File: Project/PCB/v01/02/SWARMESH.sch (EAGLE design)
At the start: 48 parts, among them IC1 4051N, M1 MOTOR10MM, M2 MOTOR10MM, Q1 TIP122, U1 ESP32DEVKITC, U2 TCRT5000L, U3 L293D, U4 7805T, U5 TCRT5000L

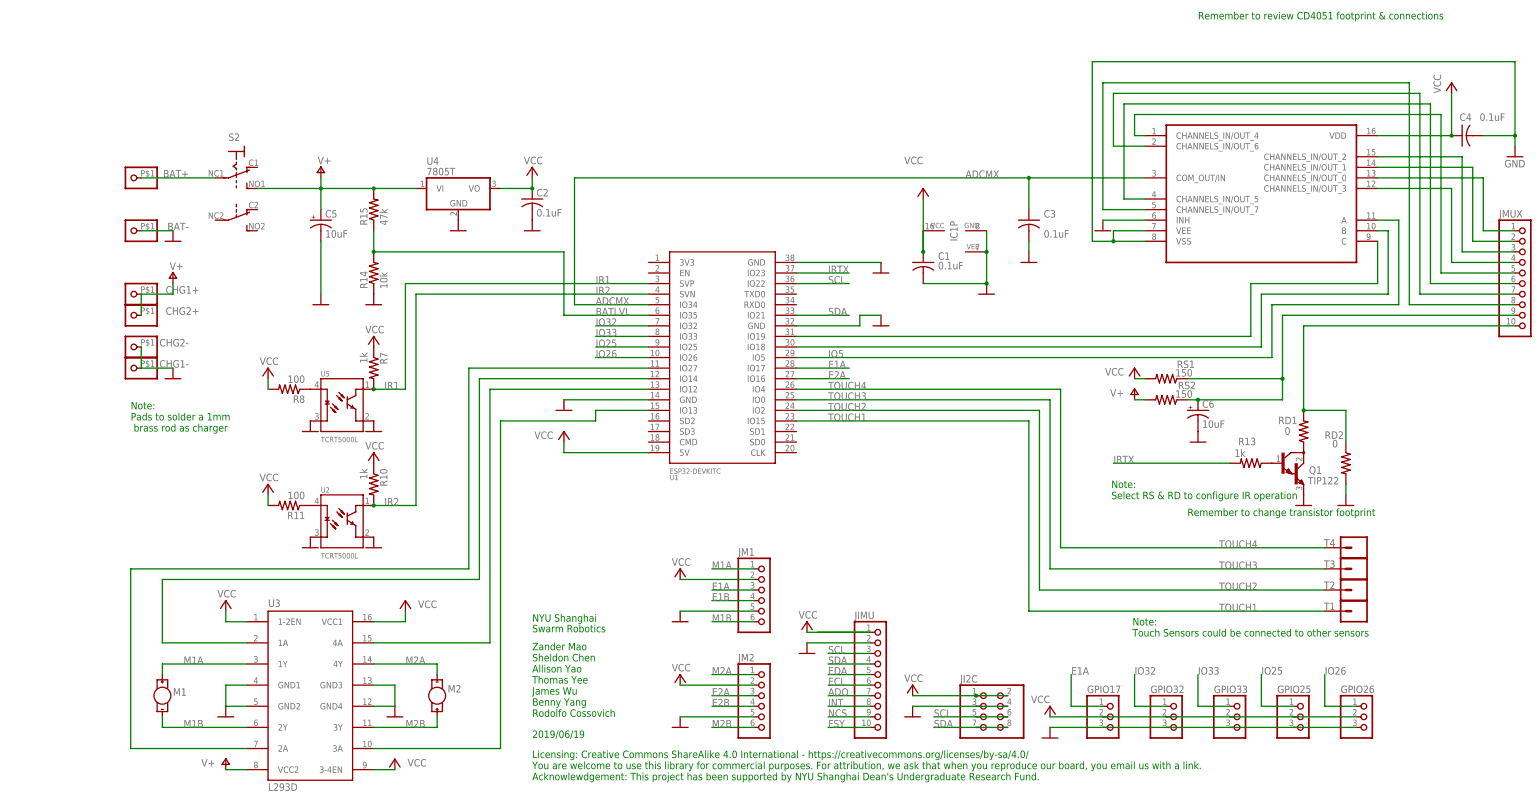
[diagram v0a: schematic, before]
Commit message: update schematic
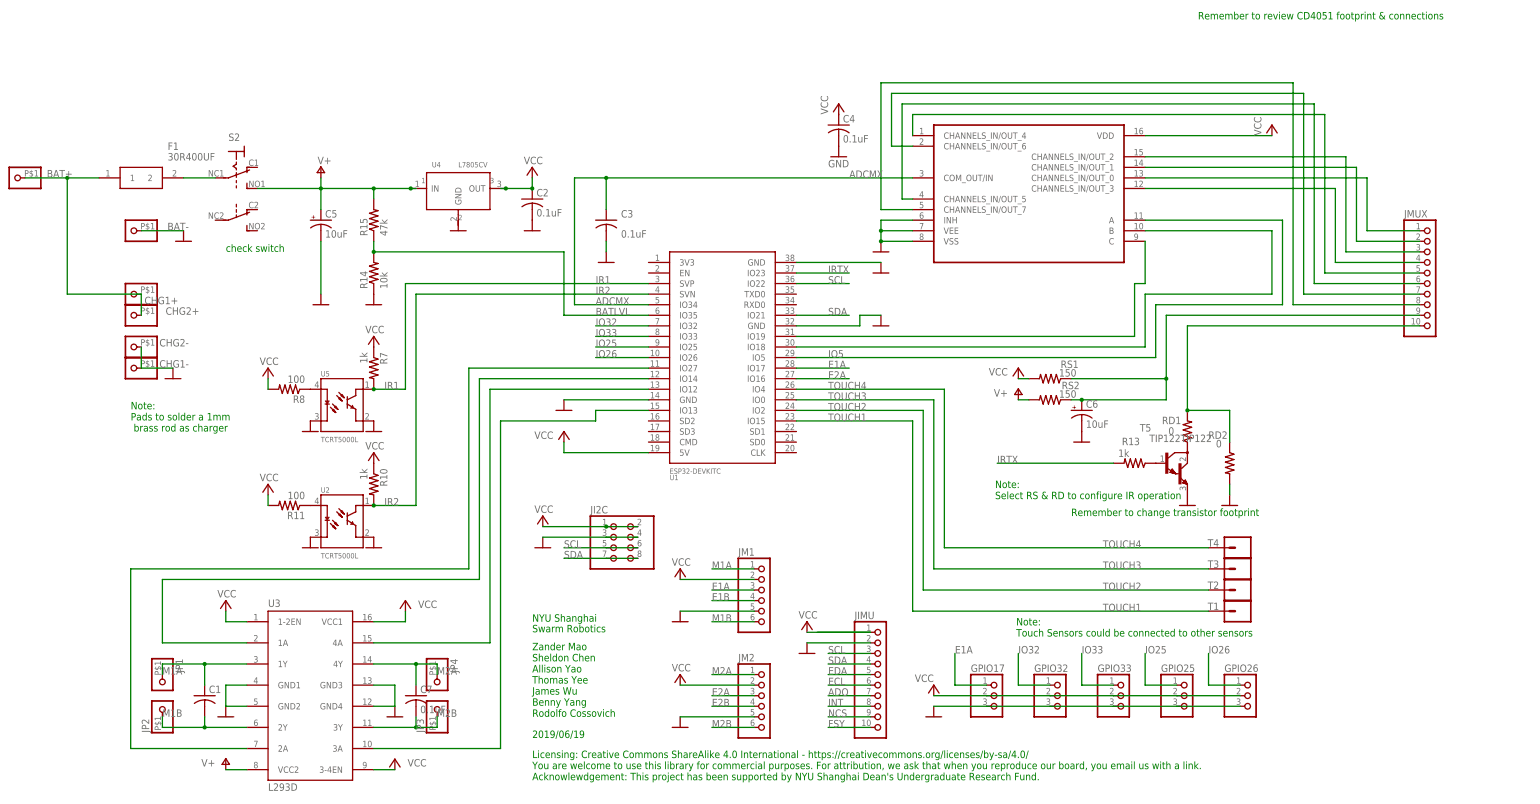
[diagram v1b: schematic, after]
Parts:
- removed IC1: 4051N, 40xx:4051N
- removed M1, M2: MOTOR10MM, SparkFun-Electromechanical:MOTOR10MM
- removed Q1: TIP122, transistor-npn:TIP122
- added C7: 0.1uF, adafruit:C-US050-024X044
- added F1: 30R400UF, 30R400UF:30R400UF
- added JP1, JP2, JP3, JP4: (no value), adafruit:PINHD-1X1-BIGPOGO
- added T5: TIP122TIP122, TIP122(2):TIP122TIP122
- C4: device adafruit:C-US050-024X044 -> rcl:C-US025-024X044
- R10, R11, R13, R14, R15, R7, R8, RD1, RD2, RS1, RS2: device adafruit:R-US_0207/12 -> adafruit:R-US_M0805
- U4: value 7805T -> L7805CV; device adafruit:7805T -> L7805:L7805CV
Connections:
- removed net N$21: BAT+.1, S21.P
- removed net N$37: Q1.C, RD1.1
- removed net N$38: R15.2
- new net N$12: R13.1, T5.B
- new net N$15: BAT+.1, CHG1+.1, CHG2+.1, F1.1
- new net N$18: F1.2, S21.P
- net GND: now also T5.E; no longer C1.2, IC1P.GND, IC1P.VEE, Q1.E, U4.GND
- net M1A: now also C1.1, JP1.1; no longer M1.+
- net M1B: now also C1.2, JP2.1; no longer M1.-
- net M2A: now also C7.1, JP4.1; no longer M2.-
- net M2B: now also C7.2, JP3.1; no longer M2.+
- net N$1: now also RD1.1, T5.C; no longer Q1.B, R13.1
- net V+: now also R15.2, U4.IN; no longer CHG1+.1, CHG2+.1, U4.VI
- net VCC: now also U4.OUT; no longer C1.1, IC1P.VCC, U4.VO
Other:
- note added: "check switch"
- moved on the sheet: BAT+, C1, C3, C4, C6, GPIO17, GPIO25, GPIO26, GPIO32, GPIO33, JI2C, JMUX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

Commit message: minor update
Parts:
- removed U$1: CD4051BEE4, CD4051BEE4:CD4051BEE4
- added U6: CD4051BEE4, CD4051BEE4:CD4051BEE4
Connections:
- removed net N$2: JMUX.1, U$1.CHANNELS_IN/OUT_0
- removed net N$3: JMUX.2, U$1.CHANNELS_IN/OUT_1
- removed net N$4: JMUX.3, U$1.CHANNELS_IN/OUT_2
- removed net N$6: JMUX.4, U$1.CHANNELS_IN/OUT_3
- new net ADCMX1: U6.COM_OUT/IN
- new net N$19: JMUX.1, U6.CHANNELS_IN/OUT_0
- new net N$20: JMUX.2, U6.CHANNELS_IN/OUT_1
- new net N$21: JMUX.4, U6.CHANNELS_IN/OUT_3
- new net N$22: JMUX.3, U6.CHANNELS_IN/OUT_2
- net ADCMX: no longer U$1.COM_OUT/IN
- net GND: no longer U$1.INH, U$1.VEE, U$1.VSS
- net IO5: now also U6.A; no longer U$1.A
- net N$11: now also U6.CHANNELS_IN/OUT_4; no longer U$1.CHANNELS_IN/OUT_4
- net N$12: now also U6.INH, U6.VEE, U6.VSS
- net N$13: now also U6.CHANNELS_IN/OUT_6; no longer U$1.CHANNELS_IN/OUT_6
- net N$14: now also U6.CHANNELS_IN/OUT_7; no longer U$1.CHANNELS_IN/OUT_7
- net N$5: now also U6.CHANNELS_IN/OUT_5; no longer U$1.CHANNELS_IN/OUT_5
- net N$7: now also U6.B; no longer U$1.B
- net N$8: now also U6.C; no longer U$1.C
- net VCC: now also U6.VDD; no longer U$1.VDD
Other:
- moved on the sheet: C6, JMUX, R13, RD1, RD2, RS1, RS2, T5

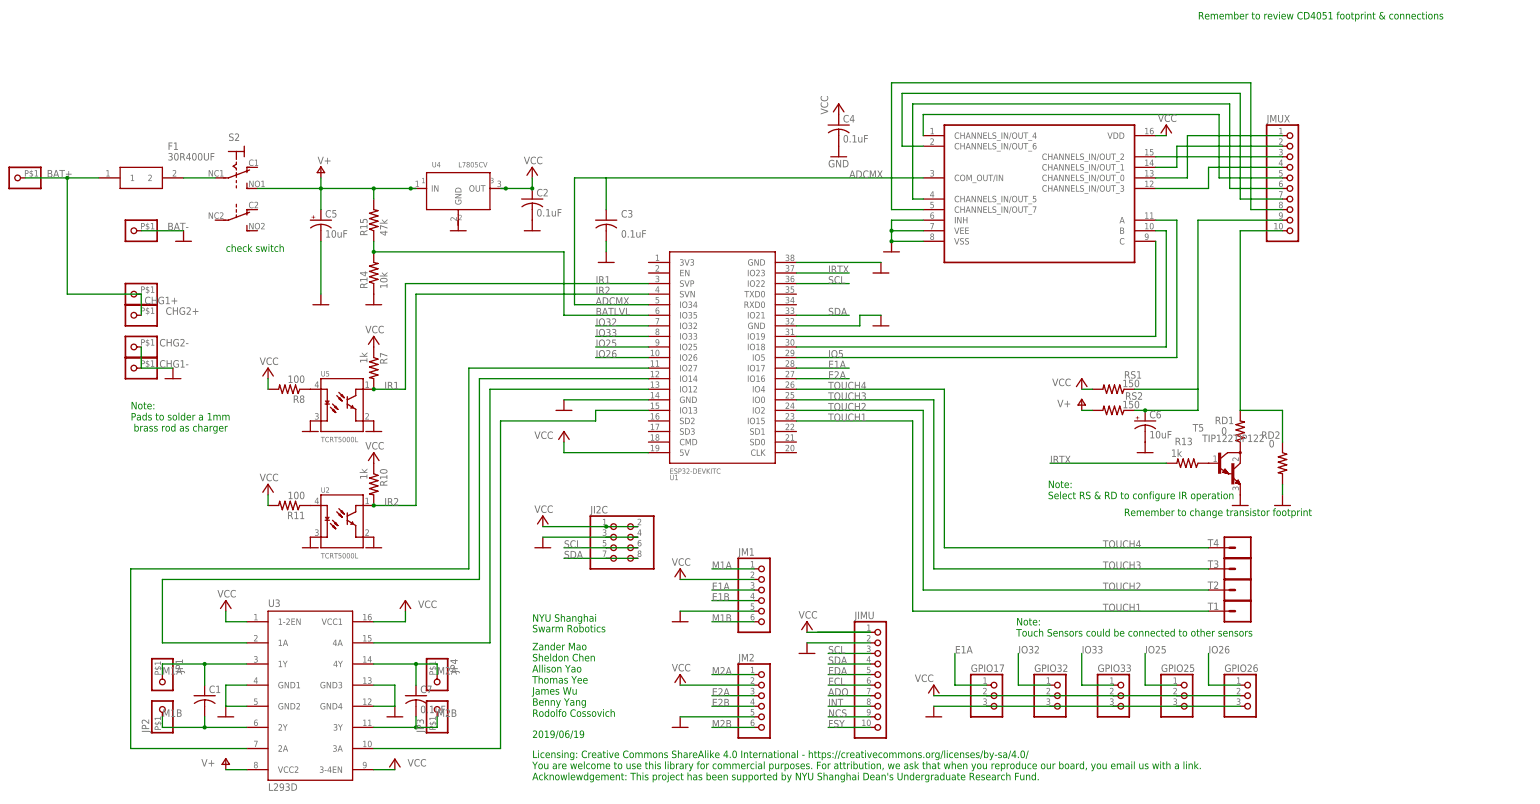
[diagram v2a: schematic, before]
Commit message: component placement
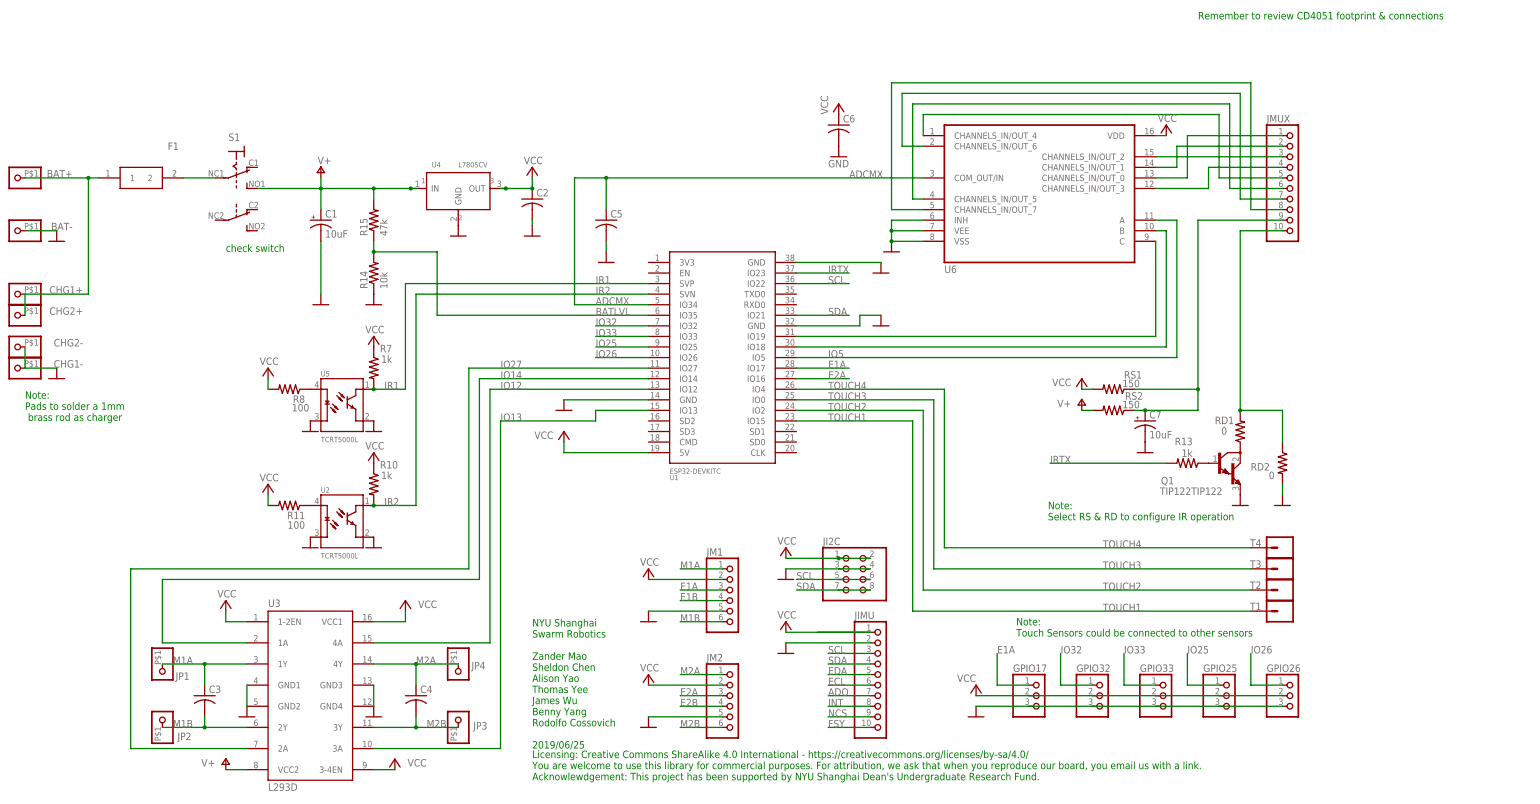
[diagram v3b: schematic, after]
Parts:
- C1, C7: value 0.1uF -> 10uF; device adafruit:C-US050-024X044 -> adafruit:CPOL-USE2.5-7
- C2, C3: value 0.1uF -> (none); device adafruit:C-US050-024X044 -> adafruit:C-USC0805
- C4: value 0.1uF -> (none); device rcl:C-US025-024X044 -> adafruit:C-USC0805
- C5, C6: value 10uF -> (none); device adafruit:CPOL-USE2.5-7 -> adafruit:C-USC0805
- renumbered S2 to S1, T5 to Q1
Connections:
- removed net ADCMX1: U6.COM_OUT/IN
- new net IO12: U1.IO12, U3.4A
- new net IO13: U1.IO13, U3.3A
- new net IO14: U1.IO14, U3.1A
- new net IO27: U1.IO27, U3.2A
- net ADCMX: now also C5.1, U6.COM_OUT/IN; no longer C3.1
- net GND: now also C1.-, C5.2, C6.2, C7.-, U4.GND; no longer C3.2, C4.2, C5.-, C6.-
- net IO5: no longer U1.IO12, U1.IO13, U1.IO14, U1.IO27, U3.1A, U3.2A, U3.3A, U3.4A
- net M1A: now also C3.1; no longer C1.1
- net M1B: now also C3.2; no longer C1.2
- net M2A: now also C4.1; no longer C7.1
- net M2B: now also C4.2; no longer C7.2
- net N$16: now also C7.+; no longer C6.+
- net V+: now also C1.+; no longer C5.+
- net VCC: now also C6.1; no longer C4.1
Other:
- note added: "NYU Shanghai Swarm Robotics Zander Mao Sheldon Chen Alison Yao Thomas Yee James Wu Benny Yang Rodolfo Cossovich 2019/06/25"
- note removed: "2019/06/19"
- note removed: "NYU Shanghai"
- note removed: "Remember to change transistor footprint"
- note removed: "Swarm Robotics"
- note removed: "Zander Mao Sheldon Chen Allison Yao Thomas Yee James Wu Benny Yang Rodolfo Cossovich"
- moved on the sheet: BAT-, C3, C4, CHG1+, CHG1-, CHG2+, CHG2-, GPIO17, GPIO25, GPIO26, GPIO32, GPIO33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

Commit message: tested with autorouting
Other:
- note removed: "Note: Touch Sensors could be connected to other sensors"
- note removed: "Remember to review CD4051 footprint & connections"
- note removed: "check switch"
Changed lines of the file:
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@@
 You are welcome to use this library for commercial purposes. For attribution, we ask that when you reproduce our board, you email us with a link.
 Acknowlewdgement: This project has been supported by NYU Shanghai Dean's Undergraduate Research Fund.</text>
-<text x="332.74" y="187.96" size="1.778" layer="91">Remember to review CD4051 footprint &amp; connections</text>
 <text x="296.672" y="67.564" size="1.778" layer="91">Note:
 Select RS &amp; RD to configure IR operation</text>
@@
 Pads to solder a 1mm
  brass rod as charger</text>
-<text x="289.052" y="39.624" size="1.778" layer="91">Note:
-Touch Sensors could be connected to other sensors</text>
-<text x="99.06" y="132.08" size="1.778" layer="91">check switch</text>
 </plain>
 <instances>

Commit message: update win file
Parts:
- removed C7: 10uF, adafruit:CPOL-USE2.5-7
- removed RS2: 150, adafruit:R-US_M0805
- removed U4: L7805CV, L7805:L7805CV
- added IC1: L7805CV-DG, L7805CV-DG:L7805CV-DG
- C1: device adafruit:CPOL-USE2.5-7 -> adafruit:CPOL-USE2-5
- C3, C4, C6: device adafruit:C-USC0805 -> adafruit:C-US025-025X050
- C5: device adafruit:C-USC0805 -> adafruit:C-US025-030X050
- F1: value 30R400UF -> RUEF300K-2; device 30R400UF:30R400UF -> RUEF300K-2:RUEF300K-2
- Q1: value TIP122TIP122 -> TIP122; device TIP122(2):TIP122TIP122 -> TIP122:TIP122
- R10, R11, R13, R14, R15, R7, R8, RD1, RD2: device adafruit:R-US_M0805 -> adafruit:R-US_0207/9
- RS1: value 150 -> 220; device adafruit:R-US_M0805 -> adafruit:R-US_0207/9
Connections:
- net GND: now also IC1.GROUND; no longer C7.-, U4.GND
- net N$16: no longer C7.+, RS2.1
- net V+: now also IC1.INPUT; no longer RS2.2, U4.IN
- net VCC: now also IC1.OUTPUT; no longer U4.OUT
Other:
- note added: "Note: We are using 5V + 22ohm resistor to control the Emitter"
- moved on the sheet: C2
